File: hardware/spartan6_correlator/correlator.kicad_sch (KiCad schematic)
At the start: 1 part, among them U3 TART Correlator SODIMM

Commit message: Updates. Lots of them
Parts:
- added D6: D_Schottky, symbol Device:D_Schottky
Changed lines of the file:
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@@
+	)
+	(symbol
+		(lib_id "Device:D_Schottky")
+		(at 35.56 147.32 0)
+		(unit 1)
+		(exclude_from_sim no)
+		(in_bom yes)
+		(on_board yes)
+		(dnp no)
+		(fields_autoplaced yes)
+		(property "Reference" "D6"
+			(at 35.2425 140.97 0)
+			(effects
+				(font
+					(size 1.27 1.27)
+				)
+			)
+		)
+		(property "Value" "D_Schottky"
+			(at 35.2425 143.51 0)
+			(effects
+				(font
+					(size 1.27 1.27)
+				)
+			)
+		)
+		(property "Footprint" ""
+			(at 35.56 147.32 0)
+			(effects
+				(font
+					(size 1.27 1.27)
+				)
+				(hide yes)
+			)
+		)
+		(property "Datasheet" "~"
+			(at 35.56 147.32 0)
+			(effects
+				(font
+					(size 1.27 1.27)
+				)
+				(hide yes)
+			)
+		)
+		(property "Description" "Schottky diode"
+			(at 35.56 147.32 0)
+			(effects
+				(font
+					(size 1.27 1.27)
+				)
+				(hide yes)
+			)
+		)
+		(pin "1"
+		)
+		(pin "2"
+		)
+		(instances
+			(project ""
+				(path "/8ae81fb2-9453-407b-8fcb-200de484ec06/94f7c847-fafa-4ae1-8500-63416fae1695"
+					(reference "D6")
+					(unit 1)
+				)
+			)
+		)
 	)
 	(symbol

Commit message: Fix SDRAM to correct model
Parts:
- D6: footprint (none) -> Diode_SMD:D_SMA
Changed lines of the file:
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@@
 			)
 		)
-		(property "Footprint" ""
+		(property "Footprint" "Diode_SMD:D_SMA"
 			(at 35.56 147.32 0)
 			(effects

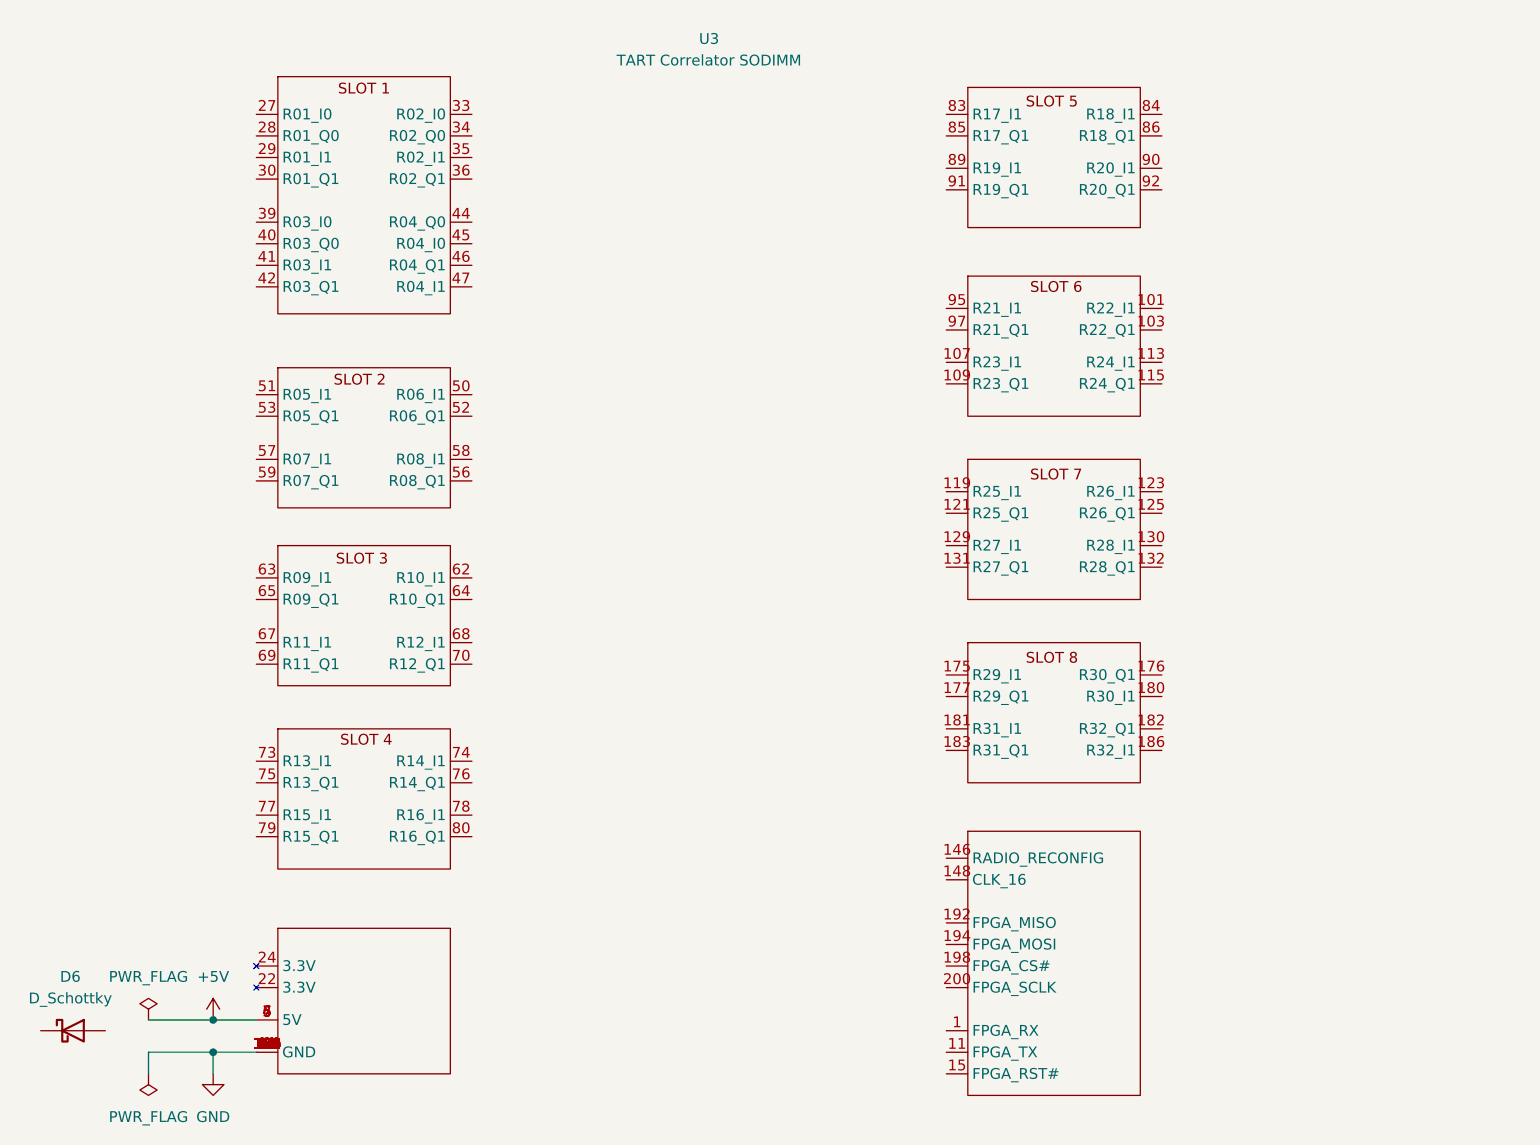
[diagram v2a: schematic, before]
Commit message: Started wiring up the radio
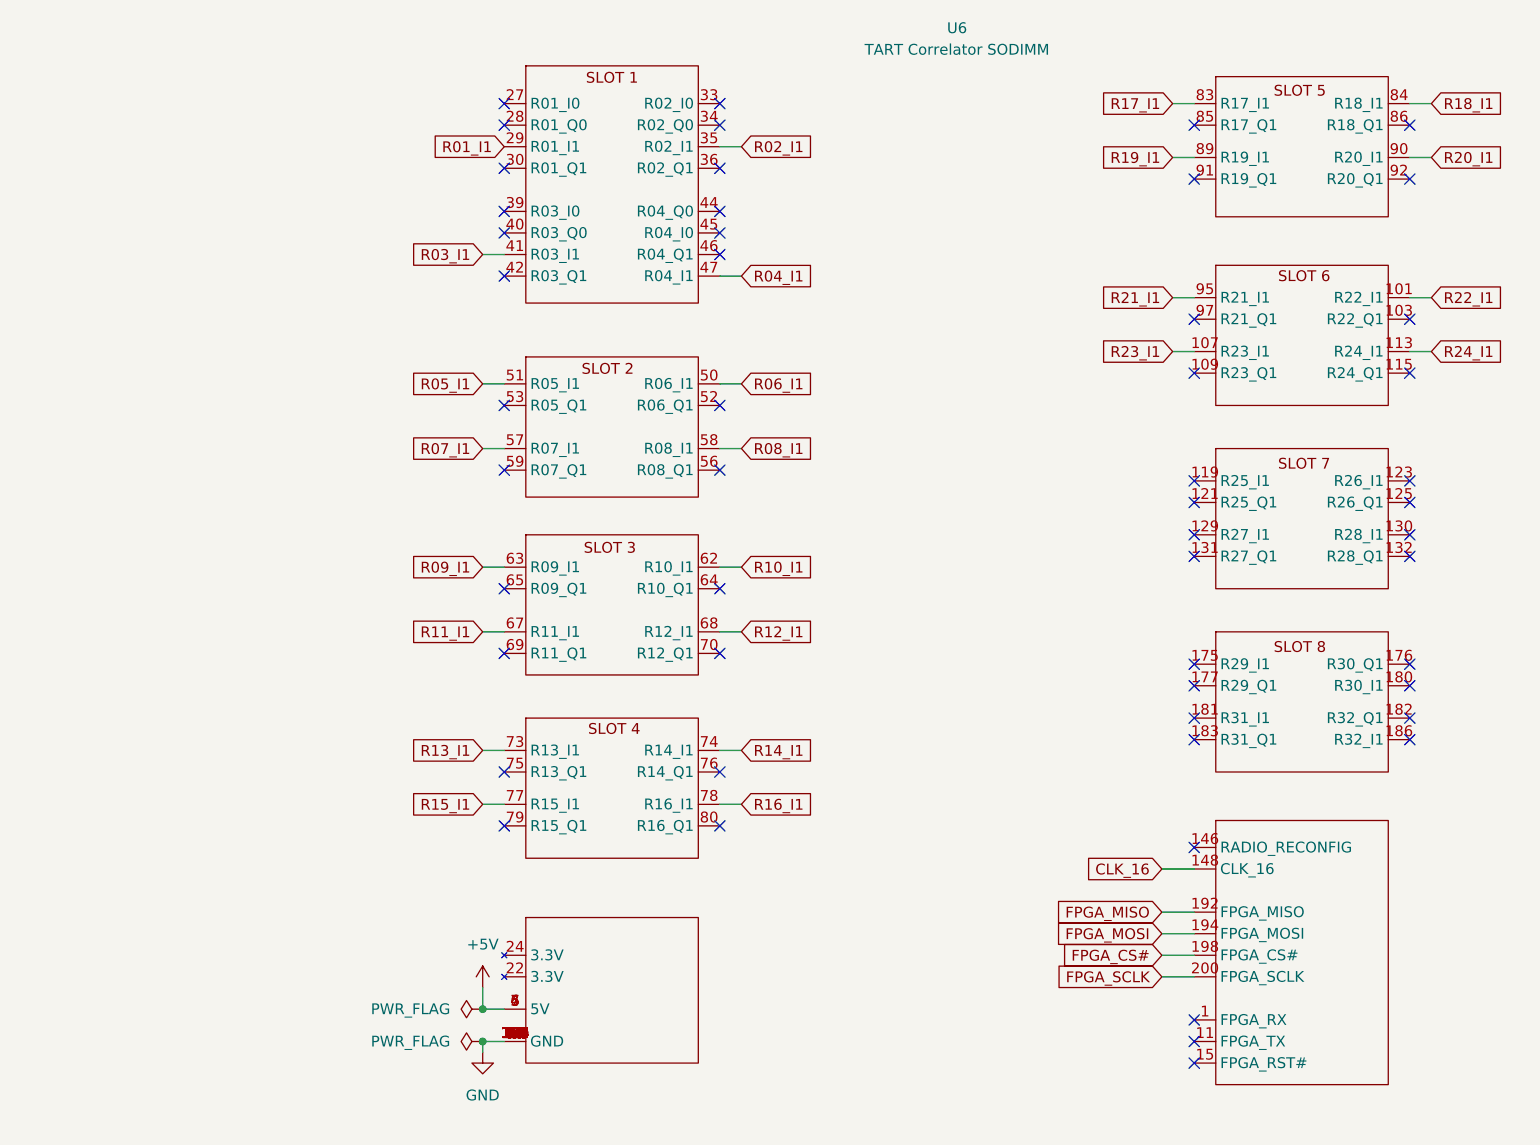
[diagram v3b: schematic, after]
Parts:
- removed D6: D_Schottky, Diode_SMD:D_SMA, symbol Device:D_Schottky
- removed U3: TART Correlator SODIMM, TART_Library:SODIMM_DDR3_EDGE, symbol TART_Library:TART_Correlator
- added U6: TART Correlator SODIMM, TART_Library:SODIMM_DDR3_EDGE, symbol TART_Library:TART_Correlator
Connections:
- net +5V: now also U6.4 (5V), U6.5 (5V), U6.6 (5V), U6.7 (5V)
- net GND: now also U6.127 (GND), U6.128 (GND), U6.13 (GND), U6.133 (GND), U6.134 (GND), U6.138 (GND), U6.139 (GND), U6.14 (GND), U6.144 (GND), U6.145 (GND), U6.150 (GND), U6.151 (GND), U6.155 (GND), U6.156 (GND), U6.161 (GND), U6.162 (GND), U6.167 (GND), U6.168 (GND), U6.172 (GND), U6.173 (GND), U6.178 (GND), U6.179 (GND), U6.184 (GND), U6.185 (GND), U6.189 (GND), U6.19 (GND), U6.190 (GND), U6.195 (GND), U6.196 (GND), U6.2 (GND), U6.20 (GND), U6.25 (GND), U6.26 (GND), U6.3 (GND), U6.31 (GND), U6.32 (GND), U6.37 (GND), U6.38 (GND), U6.43 (GND), U6.48 (GND), U6.49 (GND), U6.54 (GND), U6.55 (GND), U6.60 (GND), U6.61 (GND), U6.66 (GND), U6.71 (GND), U6.72 (GND), U6.8 (GND), U6.9 (GND)
- new net CLK_16: U6.148 (CLK_16)
- new net FPGA_CS#: U6.198 (FPGA_CS#)
- new net FPGA_MISO: U6.192 (FPGA_MISO)
- new net FPGA_MOSI: U6.194 (FPGA_MOSI)
- new net FPGA_SCLK: U6.200 (FPGA_SCLK)
- new net R01_I1: U6.29 (R01_I1)
- new net R02_I1: U6.35 (R02_I1)
- new net R03_I1: U6.41 (R03_I1)
- new net R04_I1: U6.47 (R04_I1)
- new net R05_I1: U6.51 (R05_I1)
- new net R06_I1: U6.50 (R06_I1)
- new net R07_I1: U6.57 (R07_I1)
- new net R08_I1: U6.58 (R08_I1)
- new net R09_I1: U6.63 (R09_I1)
- new net R10_I1: U6.62 (R10_I1)
- new net R11_I1: U6.67 (R11_I1)
- new net R12_I1: U6.68 (R12_I1)
- new net R13_I1: U6.73 (R13_I1)
- new net R14_I1: U6.74 (R14_I1)
- new net R15_I1: U6.77 (R15_I1)
- new net R16_I1: U6.78 (R16_I1)
- new net R17_I1: U6.83 (R17_I1)
- new net R18_I1: U6.84 (R18_I1)
- new net R19_I1: U6.89 (R19_I1)
- new net R20_I1: U6.90 (R20_I1)
- new net R21_I1: U6.95 (R21_I1)
- new net R22_I1: U6.101 (R22_I1)
- new net R23_I1: U6.107 (R23_I1)
- new net R24_I1: U6.113 (R24_I1)
- no-connect marks 0 -> 52
